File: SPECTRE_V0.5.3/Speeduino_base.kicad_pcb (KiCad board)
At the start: 2 copper layers, 100 x 93 mm, 197 parts, among them J1 Conn_01x06_Male, J2 Conn_02x04_Odd_Even, J3 ProtoArea, Q1 AO3400, Q10 BSP78, Q11 BSP78, Q12 AO3400, Q13 BSP78, Q14 BSP78, Q15 BSP78, Q16 BSP78, Q17 BSP78, Q18 BSP78, Q19 BSP78, Q20 BSP78, Q21 BSP78, Q6 AO3400, Q7 AO3400, U1 MAX9926UAEE+, U10 MIC4427, U2 LM78M05_TO220, U3 TL431DBZ, U4 molex_48pin, U5 TJA1050, U6 MAX3232, U7 MIC4427, U8 MIC4427, U9 MIC4427

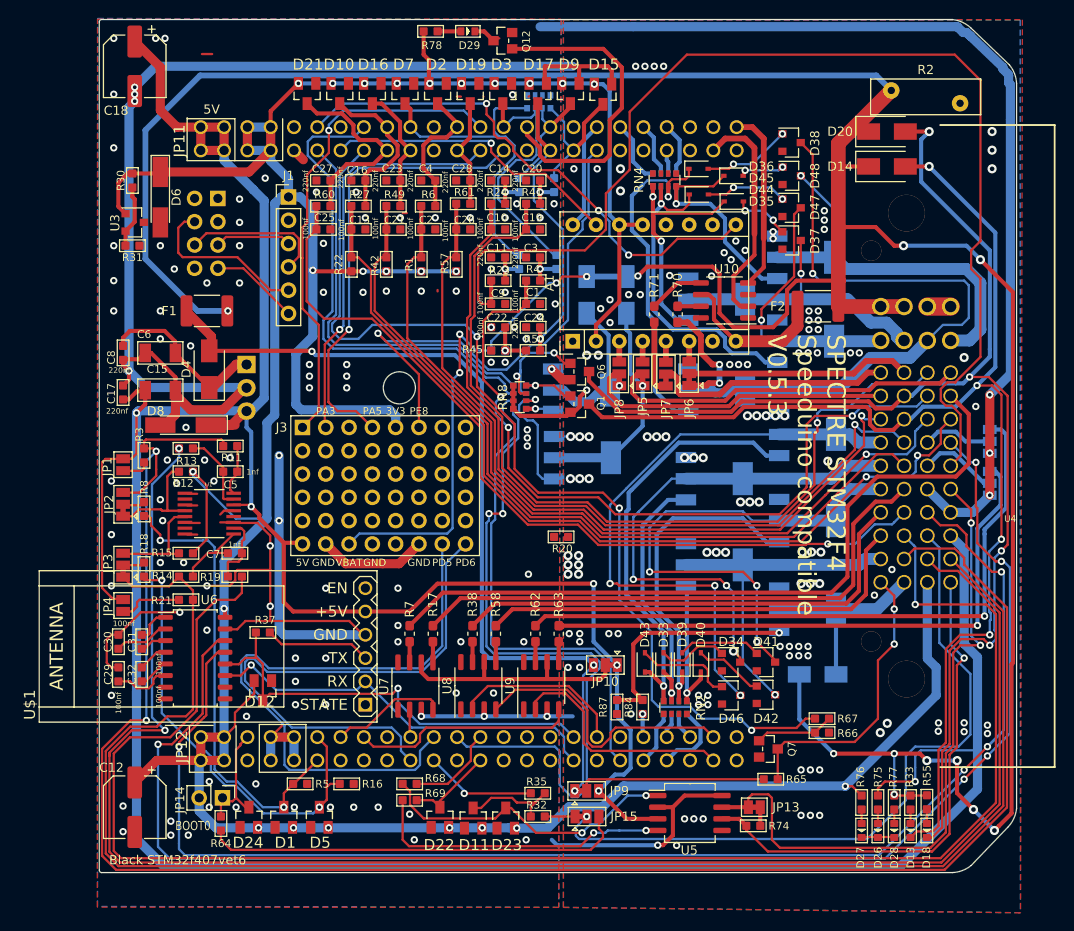
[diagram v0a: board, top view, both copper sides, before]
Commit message: Increase Vbat flyback diode trackwidth
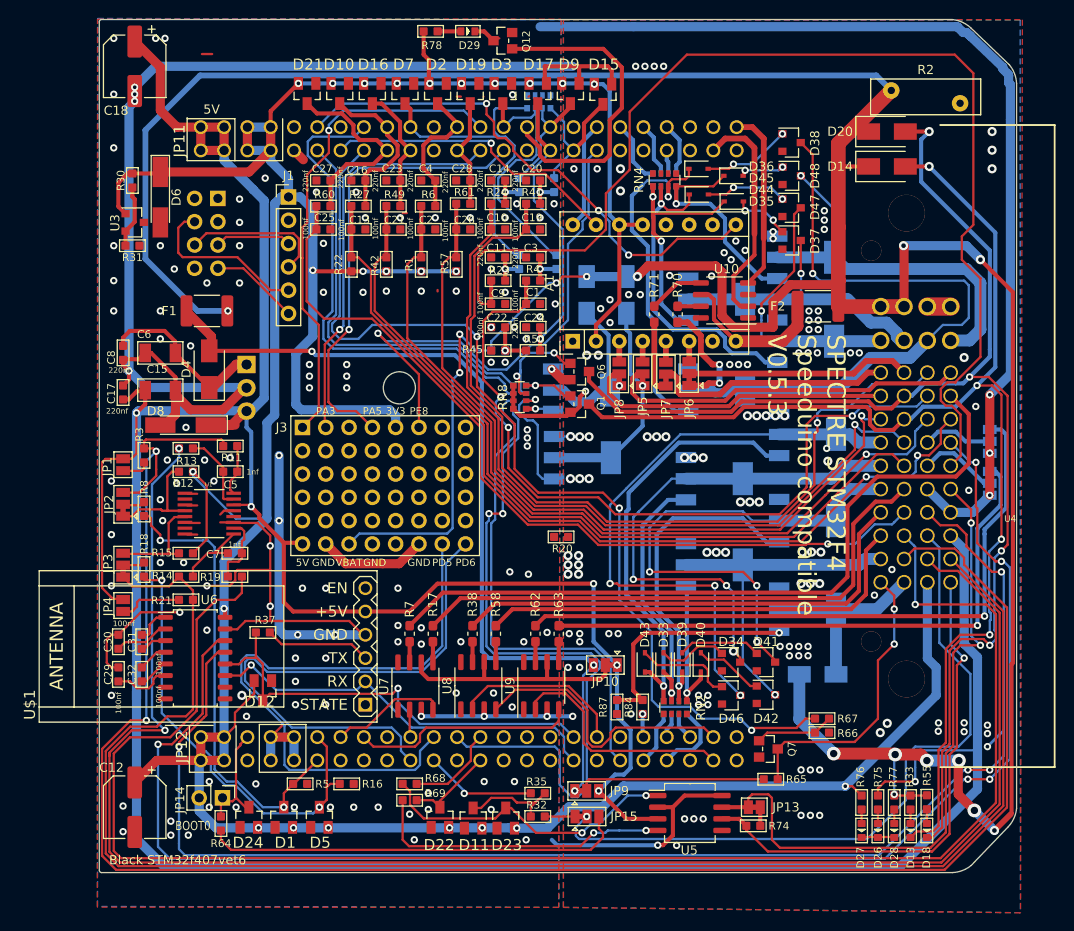
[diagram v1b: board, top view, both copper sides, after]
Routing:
- net VBAT: track 362.5 -> 371.7 mm
- net RS232_RX: track 150.8 -> 154.9 mm, vias 4 -> 5
- net RS232_TX: track 161.0 -> 162.6 mm
- net PWR_GND: vias 129 -> 131
- net INJ4-OUT: vias 3 -> 4
- net GND: vias 110 -> 124
